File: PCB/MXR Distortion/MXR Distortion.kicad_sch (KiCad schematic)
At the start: 21 parts, among them J1 Conn_01x02_Pin, J2 Conn_01x02_Pin, J3 Conn_01x02_Pin, U1 LM741

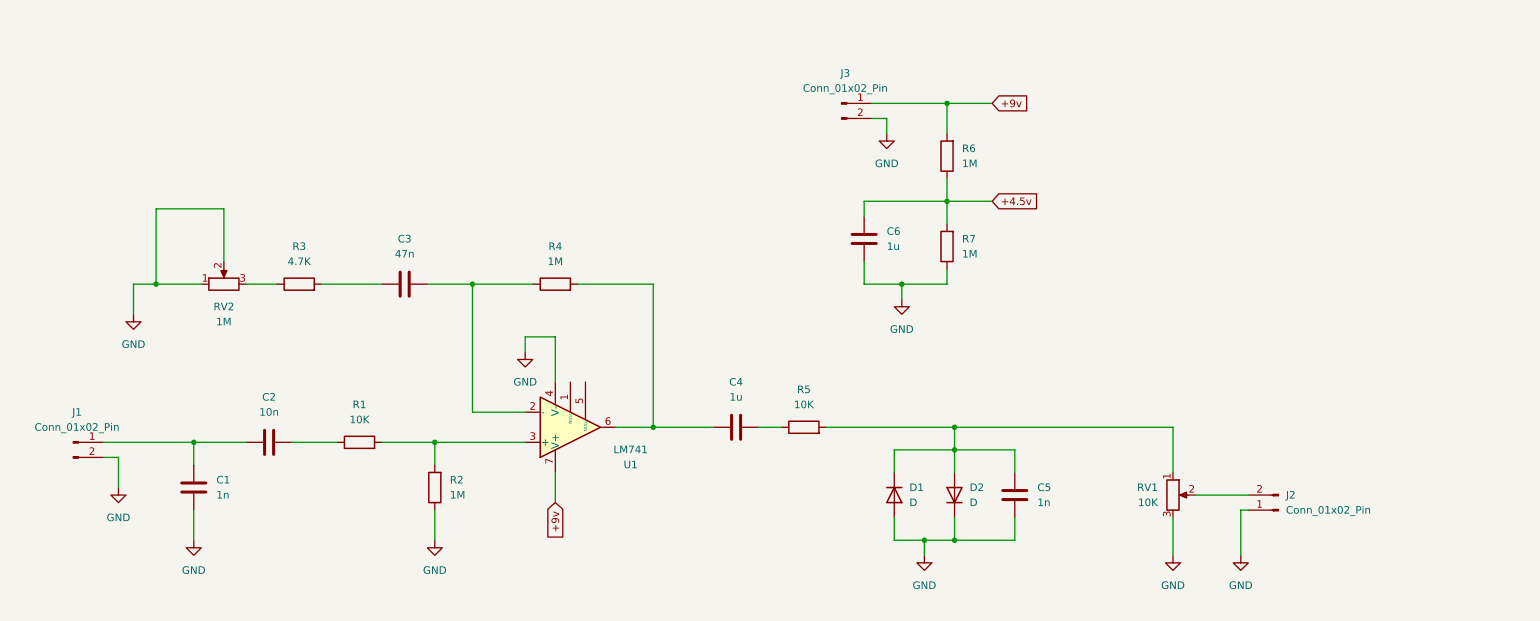
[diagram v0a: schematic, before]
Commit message: Se agrego el BOM en la carpeta Componentes y se agregaron lineas punteadas y texto al esquematico
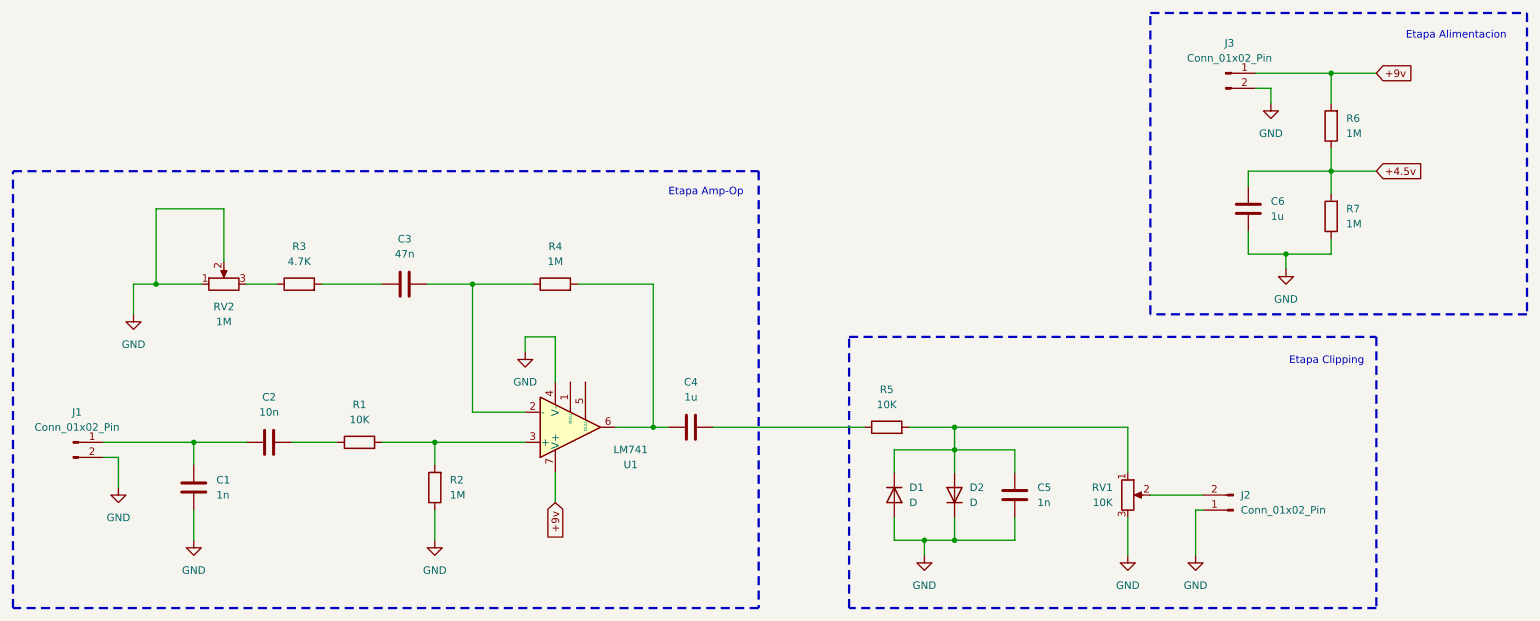
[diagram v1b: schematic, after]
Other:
- note added: "Etapa Alimentacion"
- note added: "Etapa Amp-Op"
- note added: "Etapa Clipping"
- moved on the sheet: C4, C6, J2, J3, R5, R6, R7, RV1

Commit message: Se cambiaron algunos simbolos, se agregaron los footprints y se distribuyeron las footprints en pcb
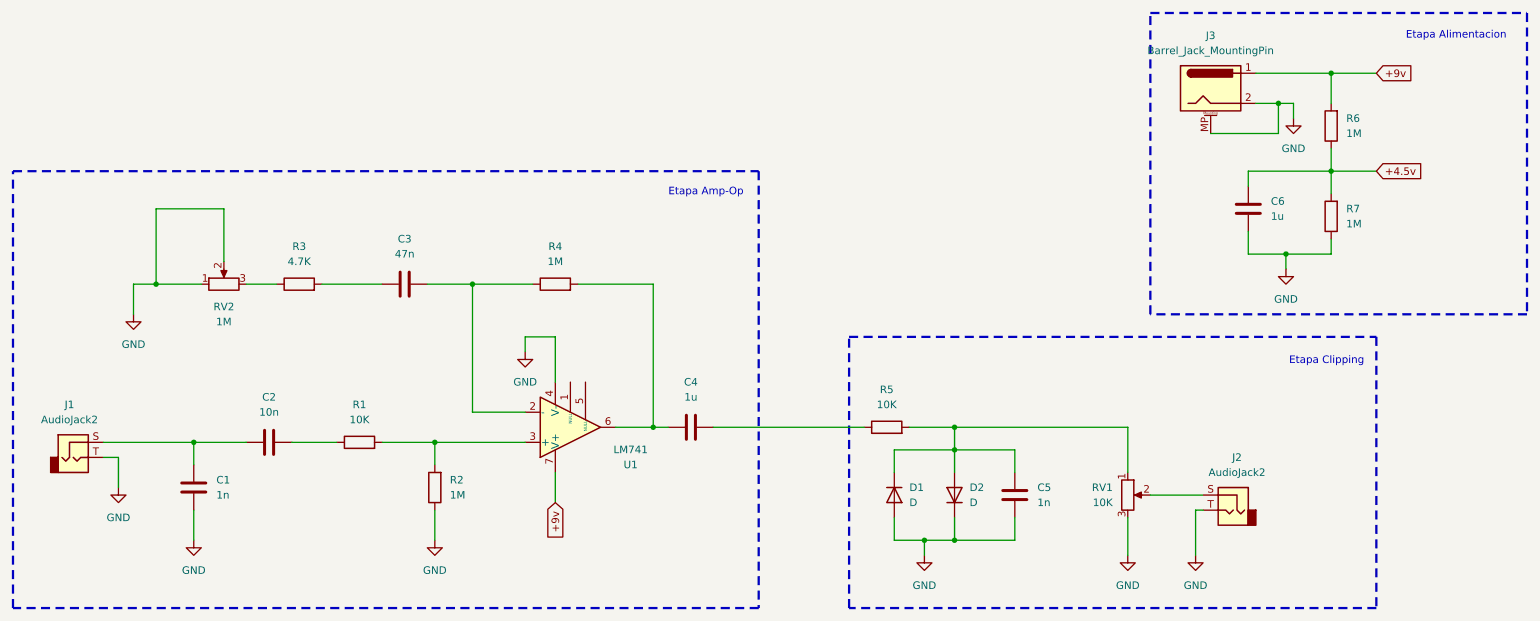
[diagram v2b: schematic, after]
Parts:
- removed J1, J2, J3: Conn_01x02_Pin, symbol Connector:Conn_01x02_Pin
- added J1, J2: AudioJack2, Connector_Audio:Jack_6.35mm_Neutrik_NMJ4HCD2_Horizontal, symbol Connector_Audio:AudioJack2
- added J3: Barrel_Jack_MountingPin, Connector_BarrelJack:BarrelJack_Horizontal, symbol Connector:Barrel_Jack_MountingPin
- C1, C5: footprint (none) -> Capacitor_THT:C_Disc_D3.0mm_W2.0mm_P2.50mm
- C2: footprint (none) -> Capacitor_THT:C_Disc_D5.0mm_W2.5mm_P5.00mm
- C3: footprint (none) -> Capacitor_THT:C_Radial_D6.3mm_H7.0mm_P2.50mm
- C4, C6: footprint (none) -> Capacitor_THT:CP_Radial_D5.0mm_P2.00mm
- D1, D2: footprint (none) -> Diode_THT:D_DO-35_SOD27_P7.62mm_Horizontal
- R1, R2, R3, R4, R5, R6, R7: footprint (none) -> Resistor_THT:R_Axial_DIN0207_L6.3mm_D2.5mm_P7.62mm_Horizontal
- RV1, RV2: footprint (none) -> Potentiometer_THT:Potentiometer_Alps_RK163_Single_Horizontal
- U1: footprint (none) -> Package_DIP:DIP-8_W7.62mm
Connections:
- net +9v: now also J3.1
- net GND: now also J1.T, J2.T, J3.2, J3.MP (MountPin)
- net at C1.2, C2.2: now also J1.S
- net at RV1.2: now also J2.S

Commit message: Simulation
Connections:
- net +4.5v: now also R2.1
- net GND: no longer R2.1
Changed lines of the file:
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@@
+		)
+	)
+	(global_label "+4.5v"
+		(shape input)
+		(at 95.25 104.14 270)
+		(fields_autoplaced yes)
+		(effects
+			(font
+				(size 1.27 1.27)
+			)
+			(justify right)
+		)
+		(property "Intersheetrefs" "${INTERSHEET_REFS}"
+			(at 95.25 112.689 90)
+			(effects
+				(font
+					(size 1.27 1.27)
+				)
+				(justify right)
+				(hide yes)
+			)
 		)
 	)
@@
 					(unit 1)
 				)
-			)
-		)
-	)
-	(symbol
-		(lib_id "power:GND")
-		(at 95.25 104.14 0)
-		(unit 1)
-		(exclude_from_sim no)
-		(in_bom yes)
-		(on_board yes)
-		(dnp no)
-		(fields_autoplaced yes)
-		(property "Reference" "#PWR02"
-			(at 95.25 110.49 0)
-			(effects
-				(font
-					(size 1.27 1.27)
-				)
-				(hide yes)
-			)
-		)
-		(property "Value" "GND"
-			(at 95.25 109.22 0)
-			(effects
-				(font
-					(size 1.27 1.27)
-				)
-			)
-		)
-		(property "Footprint" ""
-			(at 95.25 104.14 0)
-			(effects
-				(font
-					(size 1.27 1.27)
-				)
-				(hide yes)
-			)
-		)
-		(property "Datasheet" ""
-			(at 95.25 104.14 0)
-			(effects
-				(font
-					(size 1.27 1.27)
-				)
-				(hide yes)
-			)
-		)
-		(property "Description" "Power symbol creates a global label with name \"GND\" , ground"
-			(at 95.25 104.14 0)
-			(effects
-				(font
-					(size 1.27 1.27)
-				)
-				(hide yes)
-			)
-		)
-		(pin "1"
-		)
-		(instances
-			(project "MXR Distortion"
-				(path "/b557fb06-934b-48c2-9159-d15d9c76352d"
-					(reference "#PWR02")
-					(unit 1)
-				)
